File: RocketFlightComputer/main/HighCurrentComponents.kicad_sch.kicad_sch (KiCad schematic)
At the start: 23 parts, among them Q1 SI2302, Q2 SI2302, Q3 SI2302

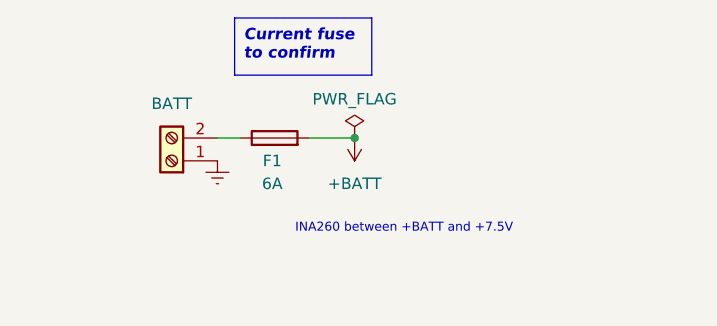
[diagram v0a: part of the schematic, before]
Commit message: Change of winbond flash to other one supported by teensy bootloader since winbond is out of stock
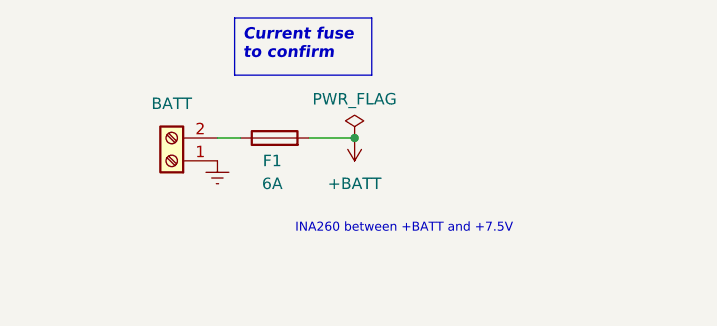
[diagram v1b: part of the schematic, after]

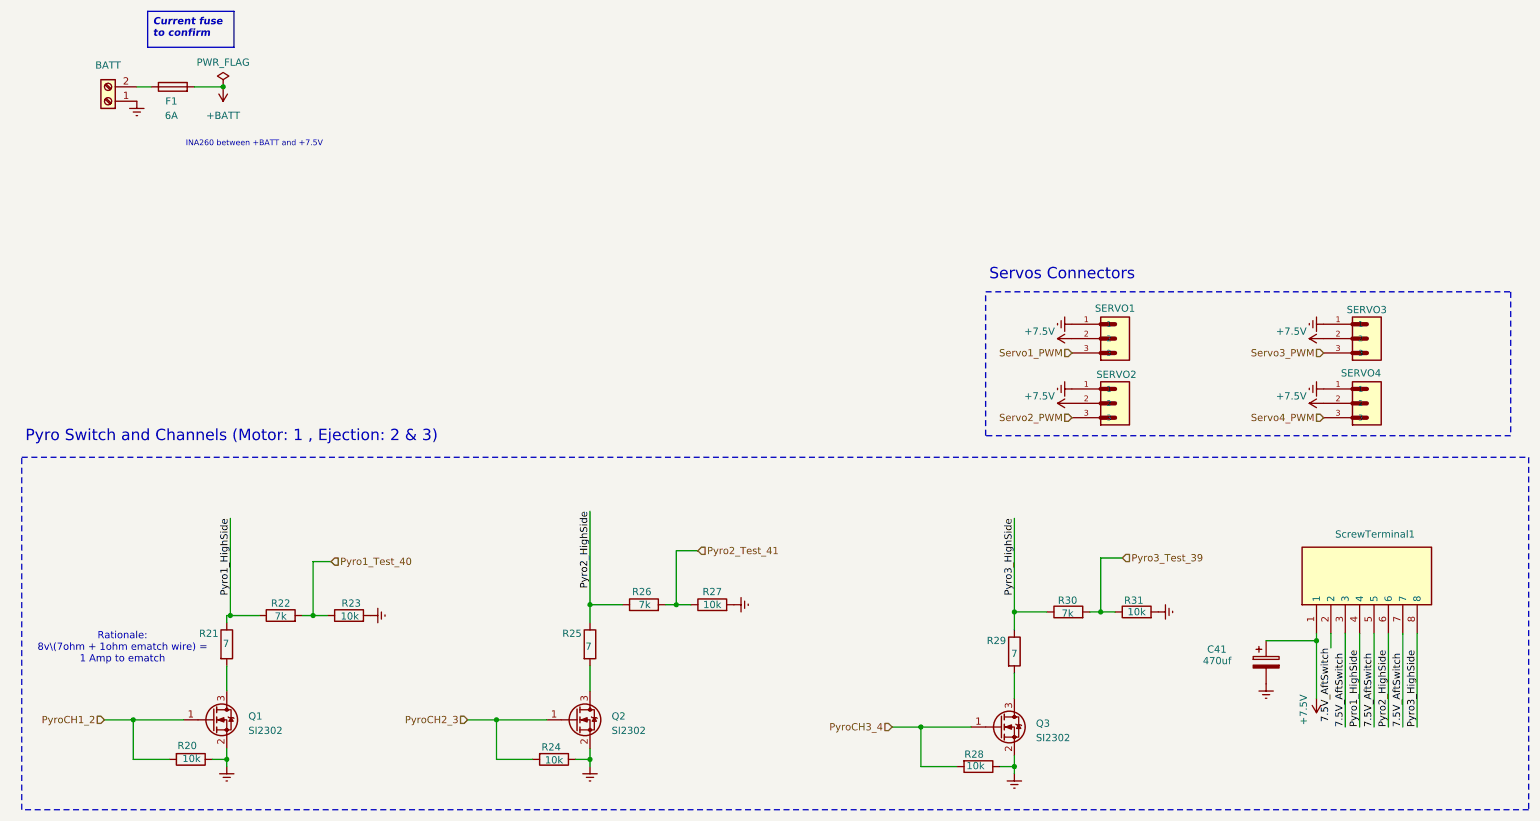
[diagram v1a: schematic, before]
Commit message: Final verification started, schematic verification of USBC and High current components
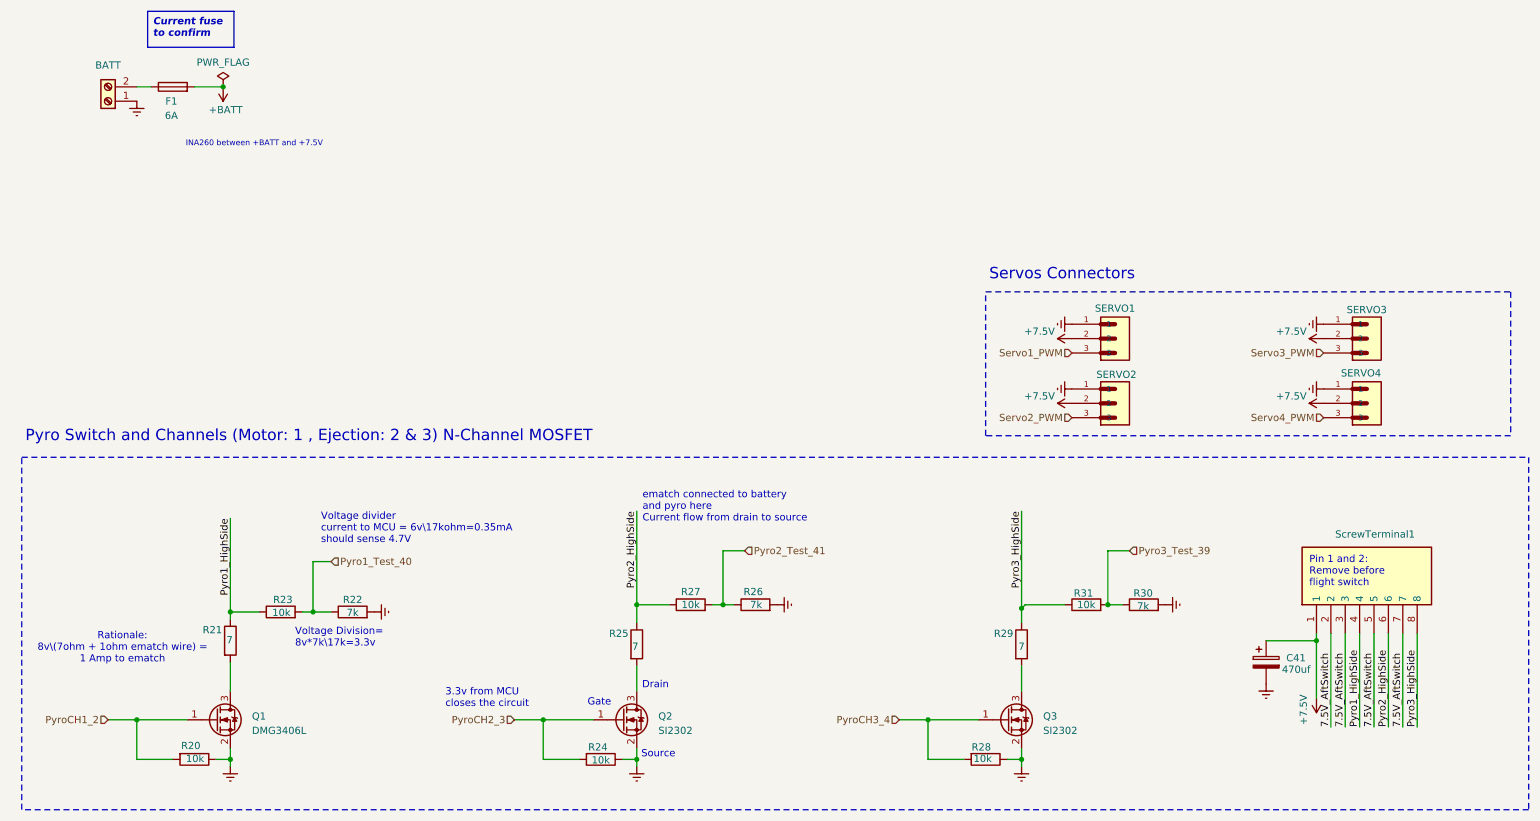
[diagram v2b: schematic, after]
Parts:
- Q1: value SI2302 -> DMG3406L
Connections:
- net GNDREF: now also R22.2, R26.2, R30.2; no longer R23.2, R27.2, R31.2
- net Pyro1_HighSide: now also R23.1; no longer R22.1
- net Pyro1_Test_40: now also R22.1, R23.2; no longer R22.2, R23.1
- net Pyro2_HighSide: now also R27.1; no longer R26.1
- net Pyro2_Test_41: now also R26.1, R27.2; no longer R26.2, R27.1
- net Pyro3_HighSide: now also R31.1; no longer R30.1
- net Pyro3_Test_39: now also R30.1, R31.2; no longer R30.2, R31.1
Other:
- note added: "3.3v from MCU closes the circuit"
- note added: "Drain"
- note added: "Gate"
- note added: "Pin 1 and 2: Remove before flight switch"
- note added: "Pyro Switch and Channels (Motor: 1 , Ejection: 2 & 3) N-Channel MOSFET"
- note added: "Source"
- note added: "Voltage Division= 8v*7k\17k=3.3v"
- note added: "Voltage divider current to MCU = 6v\17kohm=0.35mA should sense 4.7V"
- note added: "ematch connected to battery and pyro here Current flow from drain to source"
- note removed: "Pyro Switch and Channels (Motor: 1 , Ejection: 2 & 3)"
- moved on the sheet: Q1, Q2, Q3, R20, R21, R24, R25, R28, R29

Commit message: Corrected a few subsystems
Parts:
- R22, R26: value 7k -> 10k
- R23, R27, R31: value 10k -> 7k
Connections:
- net GNDREF: now also R23.2, R27.2, R31.2; no longer R22.2, R26.2, R30.2
- net Pyro1_HighSide: now also R22.1; no longer R23.1
- net Pyro1_Test_40: now also R22.2, R23.1; no longer R22.1, R23.2
- net Pyro2_HighSide: now also R26.1; no longer R27.1
- net Pyro2_Test_41: now also R26.2, R27.1; no longer R26.1, R27.2
- net Pyro3_HighSide: now also R30.1; no longer R31.1
- net Pyro3_Test_39: now also R30.2, R31.1; no longer R30.1, R31.2

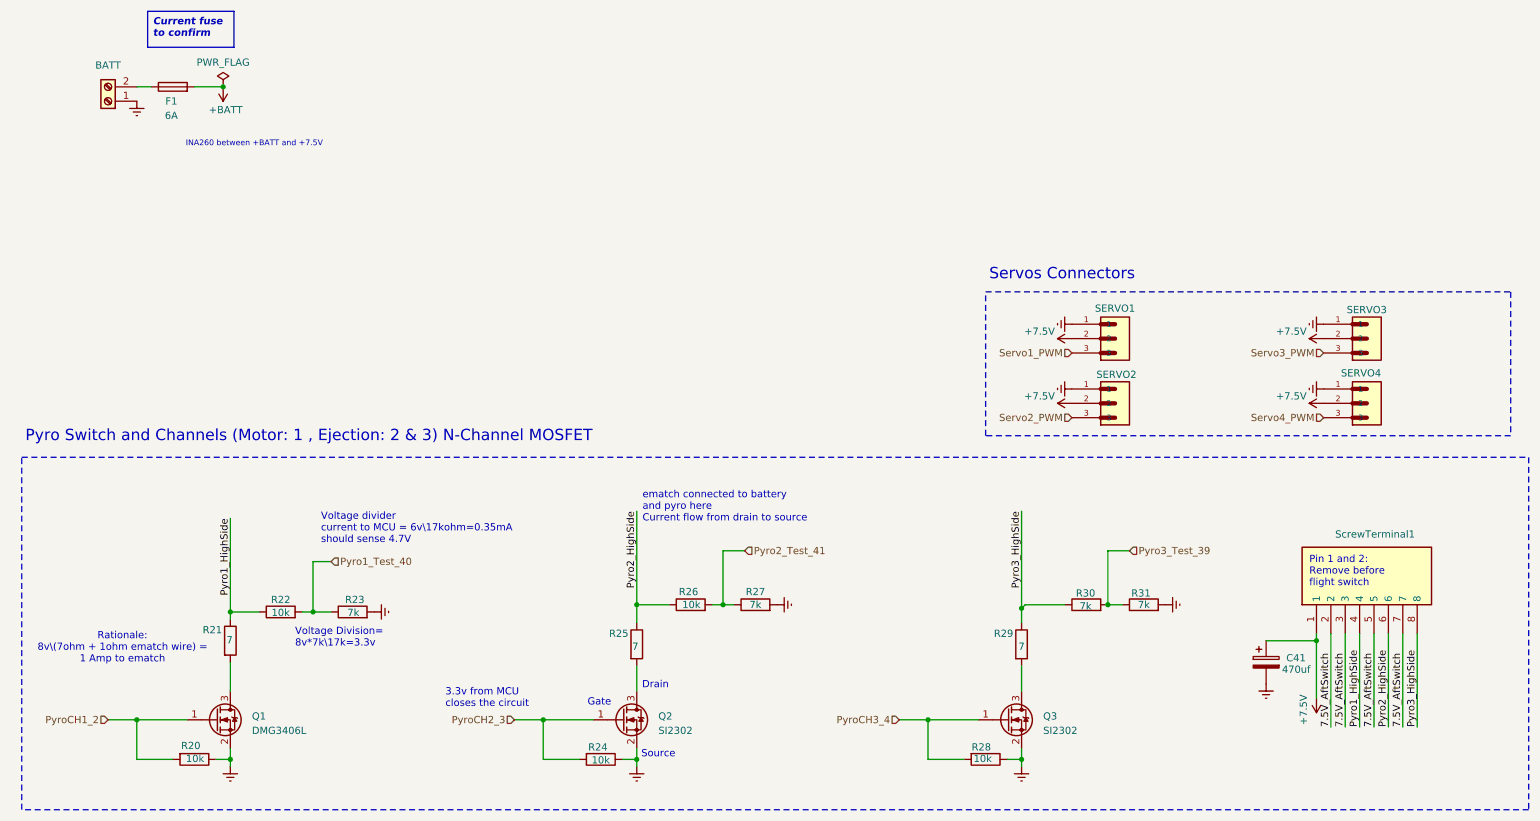
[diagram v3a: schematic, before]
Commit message: Corrections of mistake, revision of schematic is done and BOM revised, revision of pcb layout to do
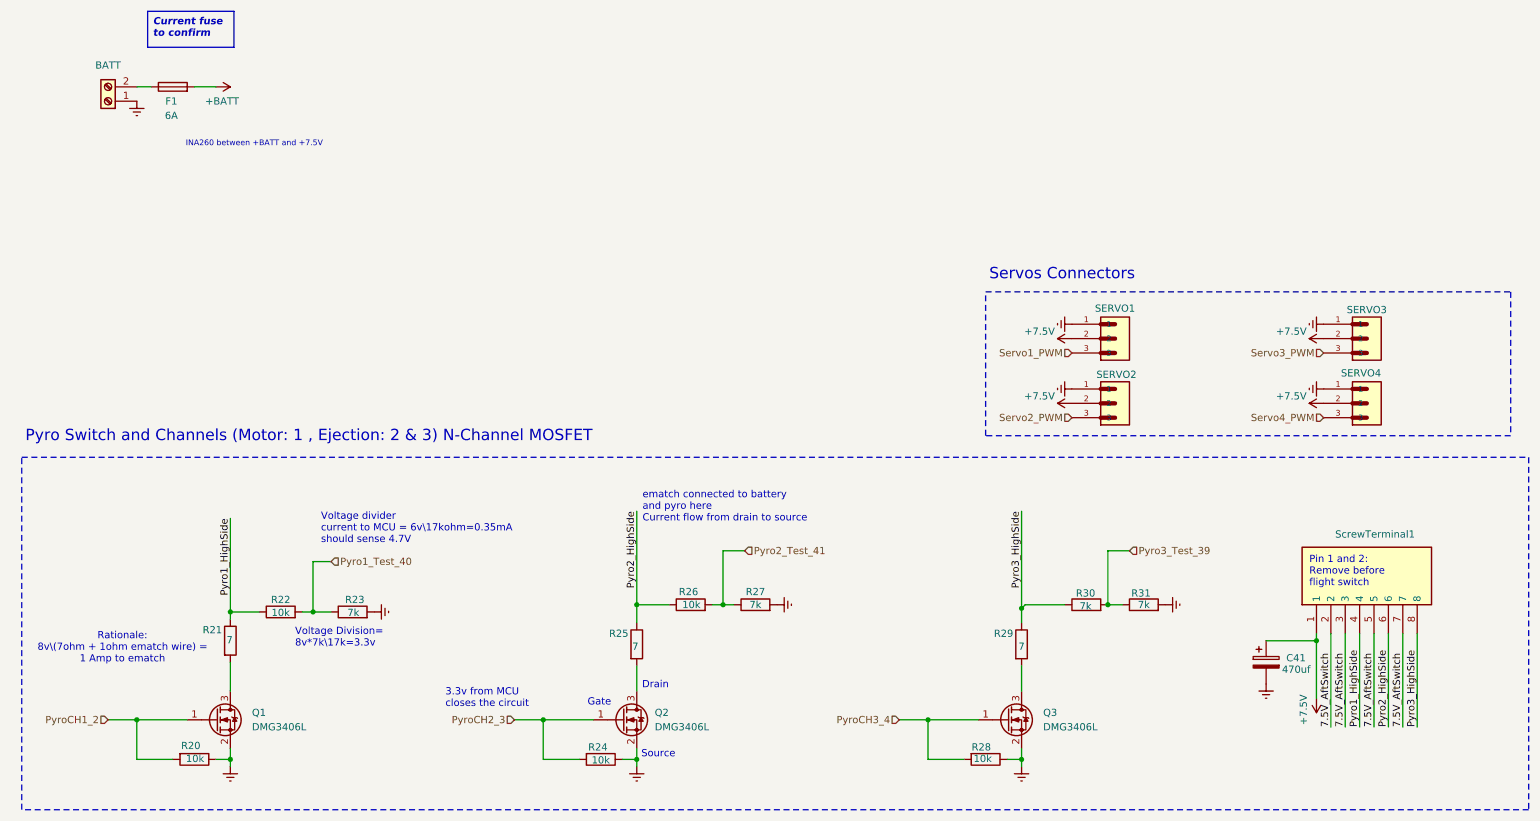
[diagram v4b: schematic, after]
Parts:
- Q2, Q3: value SI2302 -> DMG3406L
- R22, R26: LCSC C23101 -> C25804
- R23, R27, R31: LCSC C25804 -> C23101
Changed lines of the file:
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@@
 	)
 	(junction
-		(at 54.61 35.56)
-		(diameter 0)
-		(color 0 0 0 0)
-	)
-	(junction
 		(at 179.07 147.32)
 		(diameter 0)
@@
 	(wire
 		(pts
-			(xy 49.53 35.56) (xy 54.61 35.56)
+			(xy 49.53 35.56) (xy 53.34 35.56)
 		)
 		(stroke
@@
 		(fields_autoplaced yes)
 		(property "Reference" "Q1"
-			(at 59.69 146.685 0)
+			(at 59.69 146.0499 0)
 			(show_name no)
 			(do_not_autoplace no)
@@
 		)
 		(property "Value" "DMG3406L"
-			(at 59.69 149.225 0)
+			(at 59.69 148.5899 0)
 			(show_name no)
 			(do_not_autoplace no)
@@
 			)
 		)
-		(property "LCSC" "C25804 "
+		(property "LCSC" "C23101 "
 			(at 148.59 127 0)
 			(hide yes)
@@
 	)
 	(symbol
-		(lib_id "power:PWR_FLAG")
-		(at 54.61 35.56 0)
-		(unit 1)
-		(body_style 1)
-		(exclude_from_sim no)
-		(in_bom yes)
-		(on_board yes)
-		(in_pos_files yes)
-		(dnp no)
-		(property "Reference" "#FLG05"
-			(at 54.61 33.655 0)
-			(hide yes)
-			(show_name no)
-			(do_not_autoplace no)
-			(effects
-				(font
-					(size 1.27 1.27)
-				)
-			)
-		)
-		(property "Value" "PWR_FLAG"
-			(at 54.61 31.242 0)
-			(show_name no)
-			(do_not_autoplace no)
-			(effects
-				(font
-					(size 1.27 1.27)
-				)
-			)
-		)
-		(property "Footprint" ""
-			(at 54.61 35.56 0)
-			(hide yes)
-			(show_name no)
-			(do_not_autoplace no)
-			(effects
-				(font
-					(size 1.27 1.27)
-				)
-			)
-		)
-		(property "Datasheet" ""
-			(at 54.61 35.56 0)
-			(hide yes)
-			(show_name no)
-			(do_not_autoplace no)
-			(effects
-				(font
-					(size 1.27 1.27)
-				)
-			)
-		)
-		(property "Description" "Special symbol for telling ERC where power comes from"
-			(at 54.61 35.56 0)
-			(hide yes)
-			(show_name no)
-			(do_not_autoplace no)
-			(effects
-				(font
-					(size 1.27 1.27)
-				)
-			)
-		)
-		(pin "1"
-		)
-		(instances
-			(project "main"
-				(path "/27195d1d-92b2-40df-ada5-3b20841577e7/03966d30-d016-427a-9db2-b49a5b43d133"
-					(reference "#FLG05")
-					(unit 1)
-				)
-			)
-		)
-	)
-	(symbol
 		(lib_id "Device:R")
 		(at 189.23 154.305 270)
@@
 			)
 		)
-		(property "LCSC" "C23101 "
+		(property "LCSC" "C25804 "
 			(at 64.77 128.27 0)
 			(hide yes)
@@
 			)
 		)
-		(property "LCSC" "C25804 "
+		(property "LCSC" "C23101 "
 			(at 217.17 127 0)
 			(hide yes)
@@
 		(fields_autoplaced yes)
 		(property "Reference" "Q3"
-			(at 199.39 146.685 0)
+			(at 199.39 146.0499 0)
 			(show_name no)
 			(do_not_autoplace no)
@@
 			)
 		)
-		(property "Value" "SI2302"
-			(at 199.39 149.225 0)
+		(property "Value" "DMG3406L"
+			(at 199.39 148.5899 0)
 			(show_name no)
 			(do_not_autoplace no)
@@
 		(fields_autoplaced yes)
 		(property "Reference" "Q2"
-			(at 131.445 146.685 0)
+			(at 130.81 146.0499 0)
 			(show_name no)
 			(do_not_autoplace no)
@@
 			)
 		)
-		(property "Value" "SI2302"
-			(at 131.445 149.225 0)
+		(property "Value" "DMG3406L"
+			(at 130.81 148.5899 0)
 			(show_name no)
 			(do_not_autoplace no)
@@
 	(symbol
 		(lib_id "power:+BATT")
-		(at 54.61 35.56 180)
+		(at 53.34 35.56 270)
 		(unit 1)
 		(body_style 1)
@@
 		(dnp no)
 		(property "Reference" "#PWR0120"
-			(at 54.61 31.75 0)
+			(at 49.53 35.56 0)
 			(hide yes)
 			(show_name no)
@@
 		)
 		(property "Value" "+BATT"
-			(at 52.07 39.624 0)
+			(at 57.404 38.1 90)
 			(show_name no)
 			(do_not_autoplace no)
@@
 		)
 		(property "Footprint" ""
-			(at 54.61 35.56 0)
+			(at 53.34 35.56 0)
 			(hide yes)
 			(show_name no)
@@
 		)
 		(property "Datasheet" ""
-			(at 54.61 35.56 0)
+			(at 53.34 35.56 0)
 			(hide yes)
 			(show_name no)
@@
 		)
 		(property "Description" "Power symbol creates a global label with name \"+BATT\""
-			(at 54.61 35.56 0)
+			(at 53.34 35.56 0)
 			(hide yes)
 			(show_name no)
@@
 			)
 		)
-		(property "LCSC" "C23101 "
+		(property "LCSC" "C25804 "
 			(at 137.16 127 0)
 			(hide yes)
@@
 			)
 		)
-		(property "LCSC" "C25804 "
+		(property "LCSC" "C23101 "
 			(at 77.47 128.27 0)
 			(hide yes)

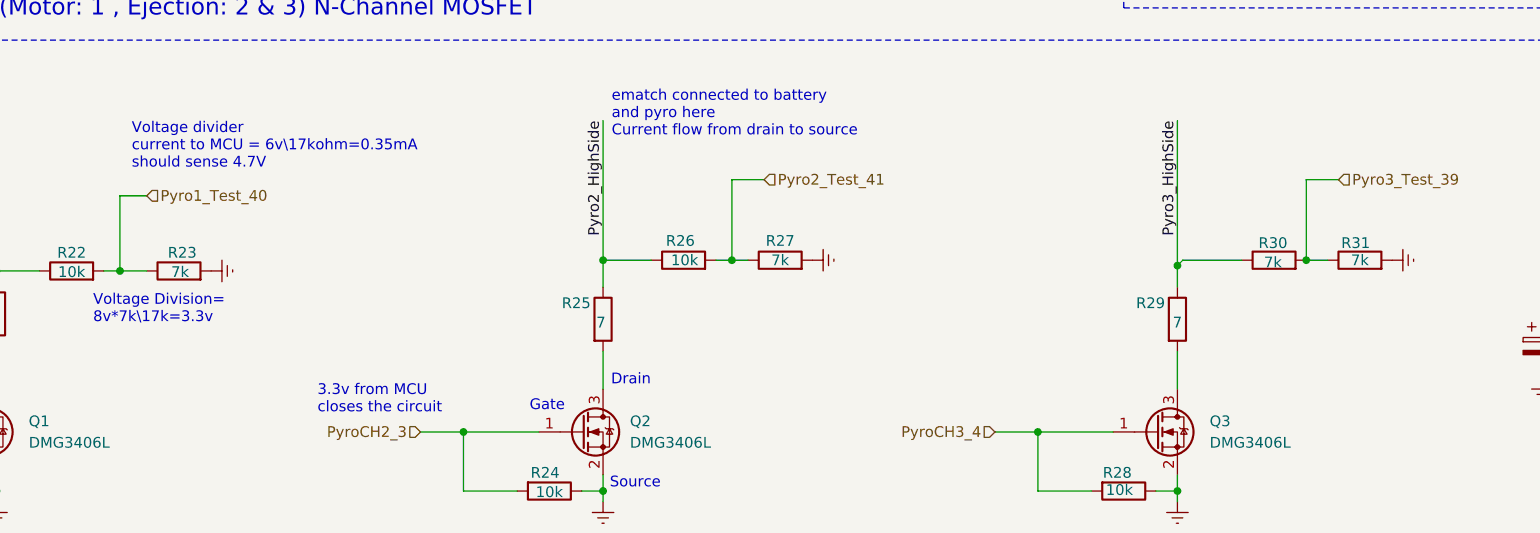
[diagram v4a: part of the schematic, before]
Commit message: Was missing pull ups on adxl375
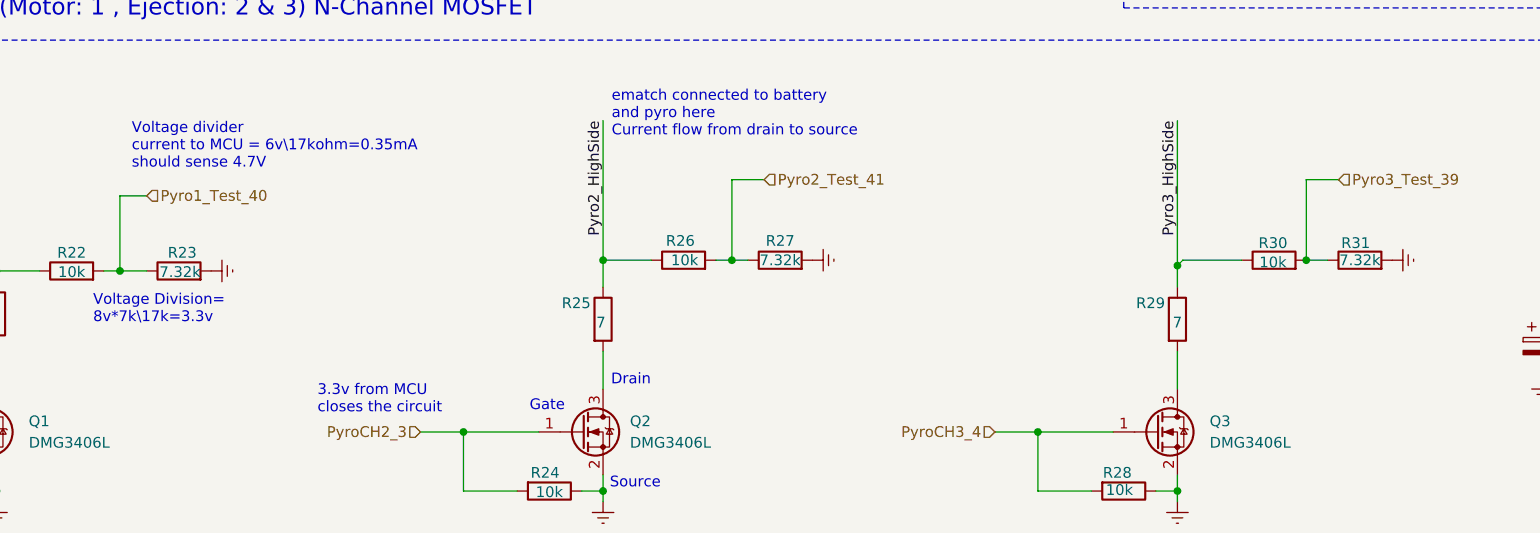
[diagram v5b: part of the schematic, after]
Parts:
- R23, R27, R31: value 7k -> 7.32k
- R30: value 7k -> 10k; LCSC C23101 -> C25804
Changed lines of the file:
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@@
 			)
 		)
-		(property "Value" "7k"
+		(property "Value" "7.32k"
 			(at 148.59 127 90)
 			(show_name no)
@@
 			)
 		)
-		(property "Value" "7k"
+		(property "Value" "10k"
 			(at 206.883 127.254 90)
 			(show_name no)
@@
 			)
 		)
-		(property "LCSC" "C23101 "
+		(property "LCSC" "C25804 "
 			(at 207.01 127 0)
 			(hide yes)
@@
 			)
 		)
-		(property "Value" "7k"
+		(property "Value" "7.32k"
 			(at 217.17 127 90)
 			(show_name no)
@@
 			)
 		)
-		(property "Value" "7k"
+		(property "Value" "7.32k"
 			(at 77.597 128.397 90)
 			(show_name no)
